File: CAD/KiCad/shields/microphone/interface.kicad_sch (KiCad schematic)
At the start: 5 parts

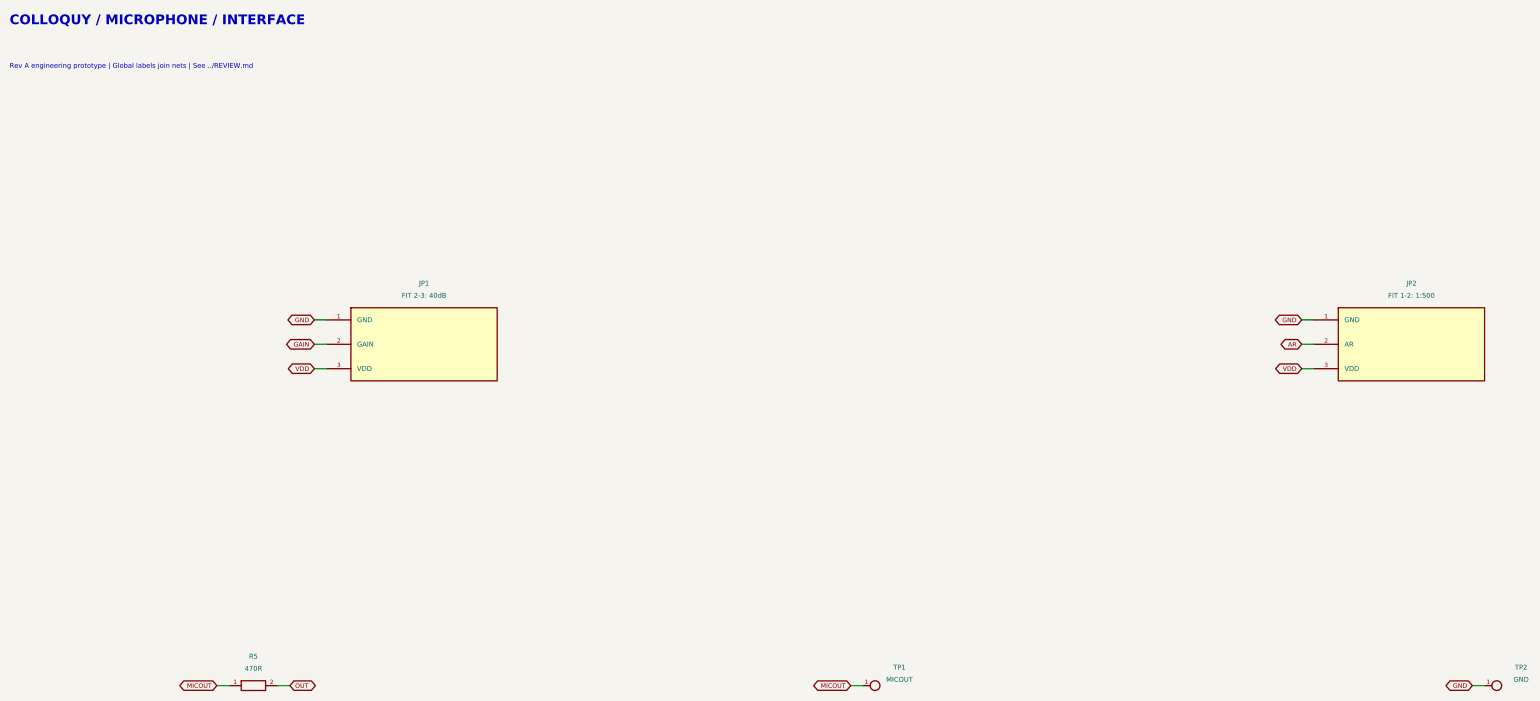
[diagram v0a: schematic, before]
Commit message: Mount the MAX9814 module on a socketed artwork holder
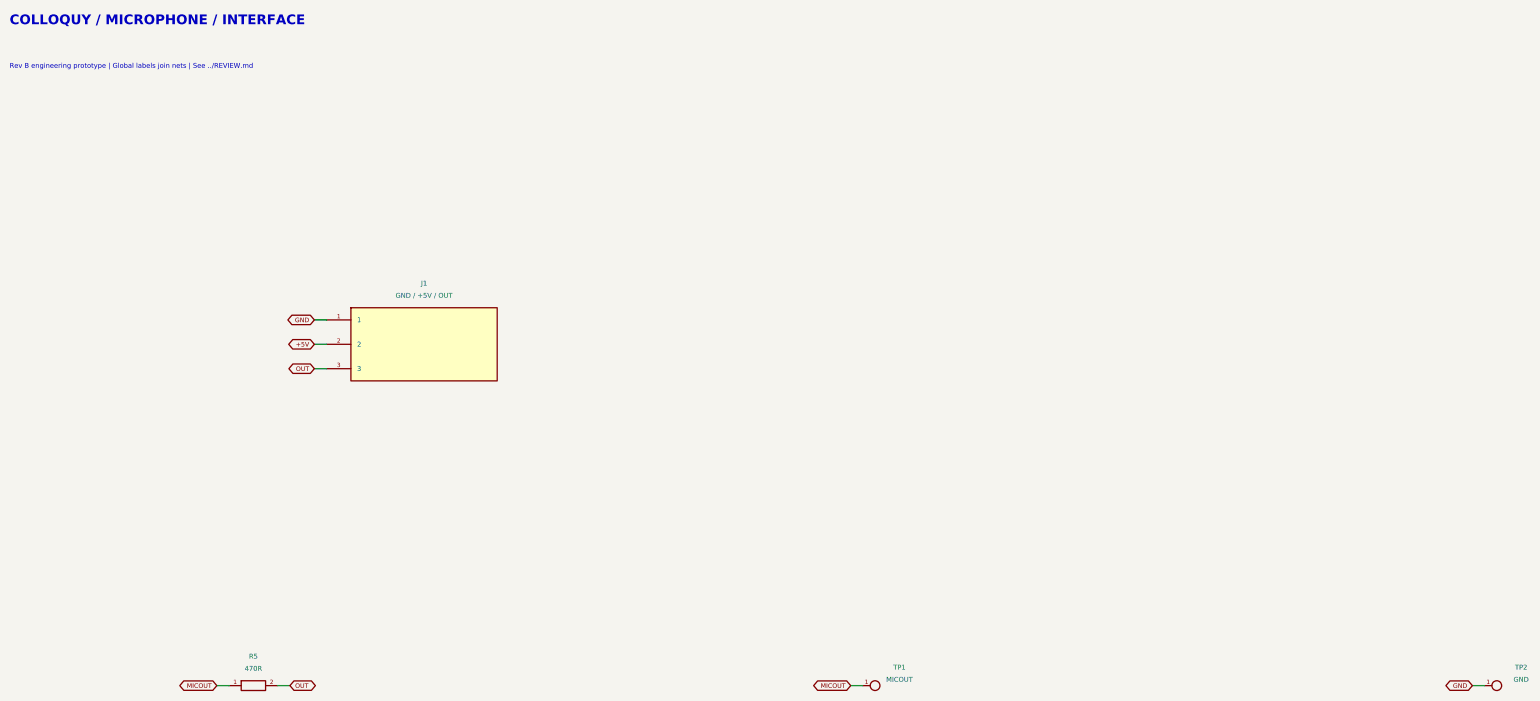
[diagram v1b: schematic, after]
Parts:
- removed JP1: FIT 2-3: 40dB, Shields:PinHeader_1x03_P2.54mm_Vertical, symbol Colloquy:JP1
- removed JP2: FIT 1-2: 1:500, Shields:PinHeader_1x03_P2.54mm_Vertical, symbol Colloquy:JP2
- added J1: GND / +5V / OUT, Shields:JST_EH_B3B-EH-A_1x03_P2.50mm_Vertical, symbol Colloquy:J1
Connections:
- net GND: now also J1.1
- net OUT: now also J1.3
- new net +5V: J1.2
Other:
- note added: "Rev B engineering prototype | Global labels join nets | See ../REVIEW.md"
- note removed: "Rev A engineering prototype | Global labels join nets | See ../REVIEW.md"
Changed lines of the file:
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@@
 (kicad_sch (version 20250114) (generator "eeschema") (generator_version "9.0")
  (paper "A3")
-          (title_block (title "microphone / interface") (date "2026-10-05") (rev "A-prototype")
+          (title_block (title "microphone / interface") (date "2026-10-08") (rev "B-module-holder")
             (company "Colloquy of Mobiles") (comment 1 "Prototype: verify harness polarity and sensor values before connection"))
           (text "COLLOQUY / MICROPHONE / INTERFACE" (at 15.24 15.24 0) (effects (font (size 2.032 2.032) (bold yes)) (justify left top)))
-(text "Rev A engineering prototype | Global labels join nets | See ../REVIEW.md" (at 15.24 25.4 0) (effects (font (size 1.016 1.016) ) (justify left top)))
-(symbol (lib_id "Colloquy:JP1") (at 101.6000 83.8200 0) (unit 1) (exclude_from_sim no) (in_bom yes) (on_board yes) (dnp no)
-(property "Reference" "JP1" (at 101.6000 71.1200 0) (effects (font (size 1.016 1.016))  ))
-(property "Value" "FIT 2-3: 40dB" (at 101.6000 73.6600 0) (effects (font (size 1.016 1.016))  ))
-(property "Footprint" "Shields:PinHeader_1x03_P2.54mm_Vertical" (at 101.6000 83.8200 0) (effects (font (size 1.27 1.27))  (hide yes)))
+(text "Rev B engineering prototype | Global labels join nets | See ../REVIEW.md" (at 15.24 25.4 0) (effects (font (size 1.016 1.016) ) (justify left top)))
+(symbol (lib_id "Colloquy:J1") (at 101.6000 83.8200 0) (unit 1) (exclude_from_sim no) (in_bom yes) (on_board yes) (dnp no)
+(property "Reference" "J1" (at 101.6000 71.1200 0) (effects (font (size 1.016 1.016))  ))
+(property "Value" "GND / +5V / OUT" (at 101.6000 73.6600 0) (effects (font (size 1.016 1.016))  ))
+(property "Footprint" "Shields:JST_EH_B3B-EH-A_1x03_P2.50mm_Vertical" (at 101.6000 83.8200 0) (effects (font (size 1.27 1.27))  (hide yes)))
 (property "Datasheet" "" (at 101.6000 83.8200 0) (effects (font (size 1.27 1.27))  (hide yes)))
-(property "Description" "Fit removable shunt: FIT 2-3: 40dB" (at 101.6000 83.8200 0) (effects (font (size 1.27 1.27))  (hide yes)))
+(property "Description" "" (at 101.6000 83.8200 0) (effects (font (size 1.27 1.27))  (hide yes)))
 (pin "1")
 (pin "2")
 (pin "3")
-(instances (project "microphone" (path "/aa568eb8-4137-509b-b6c6-b3e0a9fa148e/696c3ac1-dca8-520b-adad-1d64b64fed5e" (reference "JP1") (unit 1)))))
+(instances (project "microphone" (path "/aa568eb8-4137-509b-b6c6-b3e0a9fa148e/696c3ac1-dca8-520b-adad-1d64b64fed5e" (reference "J1") (unit 1)))))
 (wire (pts (xy 81.2800 78.7400) (xy 78.7400 78.7400)) (stroke (width 0) (type default)))
 (global_label "GND" (shape bidirectional) (at 78.7400 78.7400 180) (effects (font (size 0.95 0.95)) (justify right)) (property "Intersheetrefs" "${INTERSHEET_REFS}" (at 78.7400 78.7400 0) (effects (font (size 1.016 1.016))  (hide yes))))
 (wire (pts (xy 81.2800 83.8200) (xy 78.7400 83.8200)) (stroke (width 0) (type default)))
-(global_label "GAIN" (shape bidirectional) (at 78.7400 83.8200 180) (effects (font (size 0.95 0.95)) (justify right)) (property "Intersheetrefs" "${INTERSHEET_REFS}" (at 78.7400 83.8200 0) (effects (font (size 1.016 1.016))  (hide yes))))
+(global_label "+5V" (shape bidirectional) (at 78.7400 83.8200 180) (effects (font (size 0.95 0.95)) (justify right)) (property "Intersheetrefs" "${INTERSHEET_REFS}" (at 78.7400 83.8200 0) (effects (font (size 1.016 1.016))  (hide yes))))
 (wire (pts (xy 81.2800 88.9000) (xy 78.7400 88.9000)) (stroke (width 0) (type default)))
-(global_label "VDD" (shape bidirectional) (at 78.7400 88.9000 180) (effects (font (size 0.95 0.95)) (justify right)) (property "Intersheetrefs" "${INTERSHEET_REFS}" (at 78.7400 88.9000 0) (effects (font (size 1.016 1.016))  (hide yes))))
-(symbol (lib_id "Colloquy:JP2") (at 307.3400 83.8200 0) (unit 1) (exclude_from_sim no) (in_bom yes) (on_board yes) (dnp no)
-(property "Reference" "JP2" (at 307.3400 71.1200 0) (effects (font (size 1.016 1.016))  ))
-(property "Value" "FIT 1-2: 1:500" (at 307.3400 73.6600 0) (effects (font (size 1.016 1.016))  ))
-(property "Footprint" "Shields:PinHeader_1x03_P2.54mm_Vertical" (at 307.3400 83.8200 0) (effects (font (size 1.27 1.27))  (hide yes)))
-(property "Datasheet" "" (at 307.3400 83.8200 0) (effects (font (size 1.27 1.27))  (hide yes)))
-(property "Description" "Fit removable shunt: FIT 1-2: 1:500" (at 307.3400 83.8200 0) (effects (font (size 1.27 1.27))  (hide yes)))
-(pin "1")
-(pin "2")
-(pin "3")
-(instances (project "microphone" (path "/aa568eb8-4137-509b-b6c6-b3e0a9fa148e/696c3ac1-dca8-520b-adad-1d64b64fed5e" (reference "JP2") (unit 1)))))
-(wire (pts (xy 287.0200 78.7400) (xy 284.4800 78.7400)) (stroke (width 0) (type default)))
-(global_label "GND" (shape bidirectional) (at 284.4800 78.7400 180) (effects (font (size 0.95 0.95)) (justify right)) (property "Intersheetrefs" "${INTERSHEET_REFS}" (at 284.4800 78.7400 0) (effects (font (size 1.016 1.016))  (hide yes))))
-(wire (pts (xy 287.0200 83.8200) (xy 284.4800 83.8200)) (stroke (width 0) (type default)))
-(global_label "AR" (shape bidirectional) (at 284.4800 83.8200 180) (effects (font (size 0.95 0.95)) (justify right)) (property "Intersheetrefs" "${INTERSHEET_REFS}" (at 284.4800 83.8200 0) (effects (font (size 1.016 1.016))  (hide yes))))
-(wire (pts (xy 287.0200 88.9000) (xy 284.4800 88.9000)) (stroke (width 0) (type default)))
-(global_label "VDD" (shape bidirectional) (at 284.4800 88.9000 180) (effects (font (size 0.95 0.95)) (justify right)) (property "Intersheetrefs" "${INTERSHEET_REFS}" (at 284.4800 88.9000 0) (effects (font (size 1.016 1.016))  (hide yes))))
+(global_label "OUT" (shape bidirectional) (at 78.7400 88.9000 180) (effects (font (size 0.95 0.95)) (justify right)) (property "Intersheetrefs" "${INTERSHEET_REFS}" (at 78.7400 88.9000 0) (effects (font (size 1.016 1.016))  (hide yes))))
 (symbol (lib_id "Colloquy:R5") (at 66.0400 154.9400 0) (unit 1) (exclude_from_sim no) (in_bom yes) (on_board yes) (dnp no)
 (property "Reference" "R5" (at 66.0400 148.8440 0) (effects (font (size 1.016 1.016))  ))
